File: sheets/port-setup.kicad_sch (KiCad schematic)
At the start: 1 part

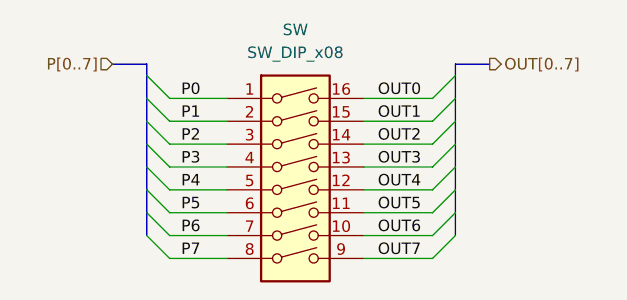
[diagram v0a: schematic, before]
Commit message: add mcu module + position components
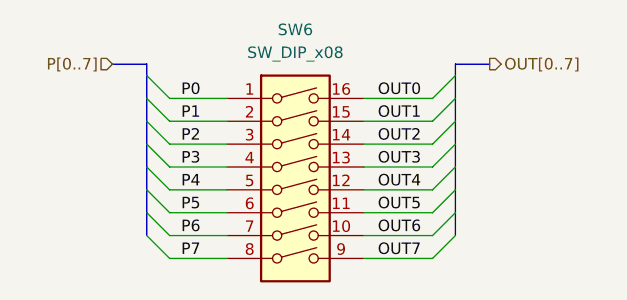
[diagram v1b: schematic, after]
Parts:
- renumbered SW to SW6
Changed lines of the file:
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@@
 		(dnp no)
 		(fields_autoplaced yes)
-		(property "Reference" "SW"
+		(property "Reference" "SW6"
 			(at 104.14 80.01 0)
 			(effects
@@
 		(instances
 			(project "esp32-didatic-kit"
+				(path "/f57920a5-fee7-4fe5-a133-e8b36941a5a6/9698fb71-dcf7-48f9-beeb-6e6a219382b5/10f00d49-e652-449c-9bf9-231ea615e92b"
+					(reference "SW6")
+					(unit 1)
+				)
 				(path "/f57920a5-fee7-4fe5-a133-e8b36941a5a6/9698fb71-dcf7-48f9-beeb-6e6a219382b5/ee6d5bfe-64f6-446c-ab84-257e42489673"
 					(reference "SW7")
